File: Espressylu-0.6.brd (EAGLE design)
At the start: 101.6 x 76.2 mm, 135 parts, among them J1 4P-TERM-BLOCK284391-4, J10 MICROSD, J11 2x7, J2 M02POLAR, J3 M02POLAR, J4 USB-MICRO-PTH, J5 M02POLAR, J6 HOTEND-1, J7 HOTBED, J8 M02POLAR, J9 M02POLAR, P1 POLOLU-X, P2 POLOLU-Y, P3 POLOLU-Z, P4 POLOLU-E1, Q1 PMV45EN, Q2 PSMN1R8-40YLC, Q3 MMUN2211LT3G, Q4 PSMN1R8-40YLC, U1 DRTR5V0U2SR, U2 MCP1402T, U3 LMR16006X, U4 L78L15ABUTR, U5 MCP1402T, X1 12MHZ

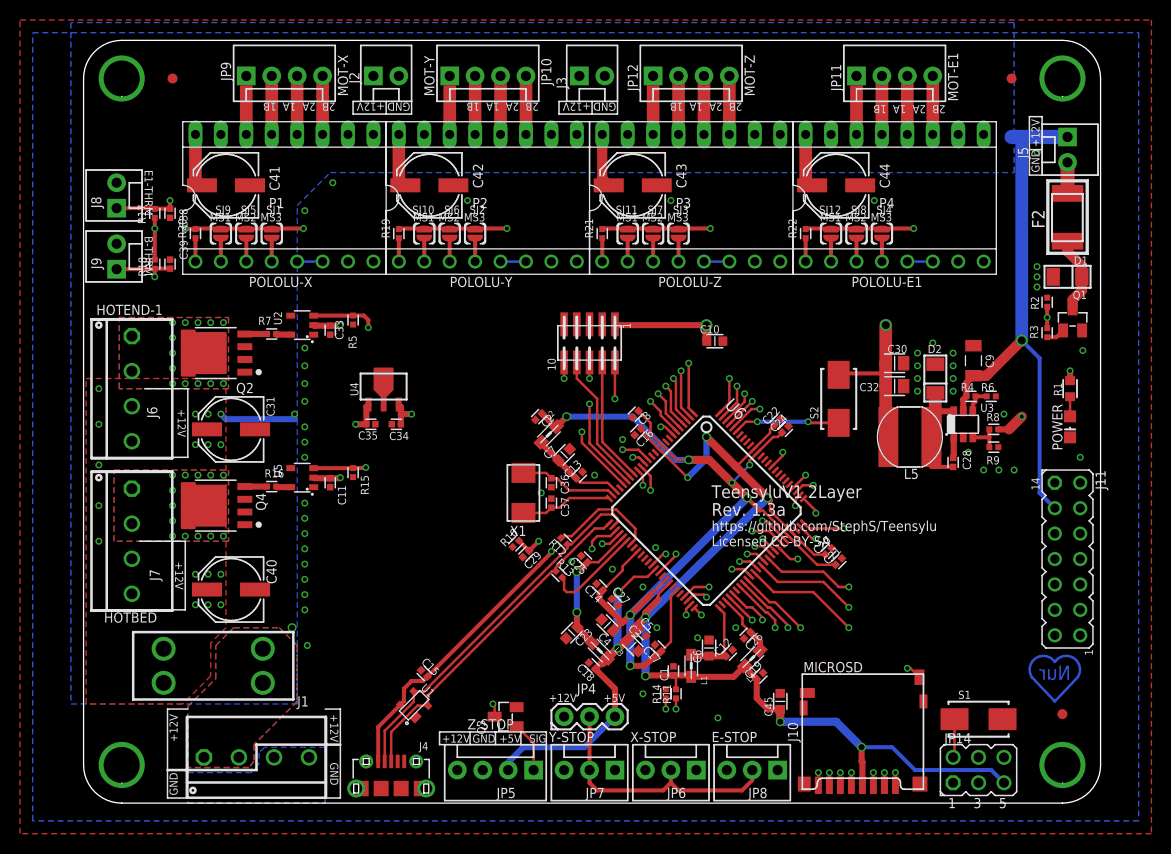
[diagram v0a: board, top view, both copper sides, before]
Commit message: Layout cleanup
Moved the stepper motor headers closer to the connectors. Cleaned up the
schematic and labels.
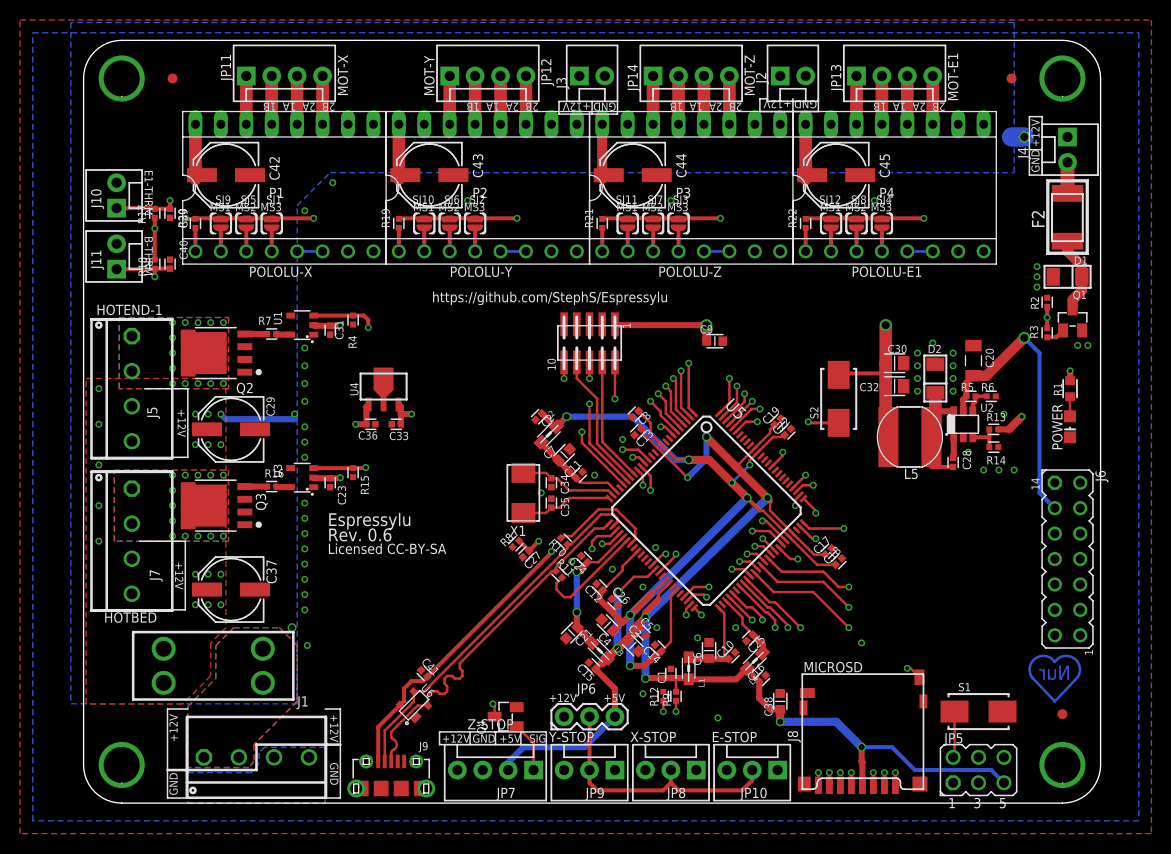
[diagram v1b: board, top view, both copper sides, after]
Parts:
- C10, C23: value 4.7uF -> 0.1uF; device teensylu:CAPC1608X92N -> teensylu:CAPC1005X60N
- C20: value 0.1uF -> 4.7uF; device teensylu:CAPC1005X60N -> teensylu:CAPC3215X168N
- C21: value 0.1uF -> 4.7uF; device teensylu:CAPC1005X60N -> teensylu:CAPC1608X92N
- C27: value 0.1uF -> 10pF
- C29: value 10pF -> 100uF; device teensylu:CAPC1005X60N -> teensylu:PANASONIC_D
- C31, C41: value 100uF -> 0.1uF; device teensylu:PANASONIC_D -> teensylu:CAPC1005X60N
- C33: value 0.1uF -> 1uF
- C34: value 1uF -> 15pF
- C35: value 0.1uF -> 15pF
- C36: value 15pF -> 0.1uF
- C37: value 15pF -> 100uF; device teensylu:CAPC1005X60N -> teensylu:PANASONIC_D
- C38: value 10uF -> 4.7uF; device teensylu:CAPC1005X60N -> teensylu:CAPC1608X92N
- C40: value 100uF -> 10uF; device teensylu:PANASONIC_D -> teensylu:CAPC1005X60N
- C45: value 4.7uF -> 100uF; device teensylu:CAPC1608X92N -> teensylu:PANASONIC_D
- C9: device teensylu:CAPC3215X168N -> teensylu:CAPC1608X92N
- J10: value MICROSD -> M02POLAR; device teensylu:AMPHENOL-MICROSD -> teensylu:MOLEX-1X2
- J11: value 2x7 -> M02POLAR; device teensylu:JP7Q -> teensylu:MOLEX-1X2
- J4: value USB-MICRO-PTH -> M02POLAR; device teensylu:USB-MICROB-PTH -> teensylu:MOLEX-1X2
- J5: value M02POLAR -> HOTEND-1; device teensylu:MOLEX-1X2 -> teensylu:284391-4
- J6: value HOTEND-1 -> 2x7; device teensylu:284391-4 -> teensylu:JP7Q
- J8: value M02POLAR -> MICROSD; device teensylu:MOLEX-1X2 -> teensylu:AMPHENOL-MICROSD
- J9: value M02POLAR -> USB-MICRO-PTH; device teensylu:MOLEX-1X2 -> teensylu:USB-MICROB-PTH
- JP10: value MOT-Y -> M03POLAR; device teensylu:MOLEX-1X4 -> teensylu:MOLEX-1X3
- JP11: value MOT-E1 -> MOT-X
- JP12: value MOT-Z -> MOT-Y
- JP13: value JTAG-HEADER -> MOT-E1; device teensylu:2X05-0.5-SMD -> teensylu:MOLEX-1X4
- JP14: value ISP -> MOT-Z; device teensylu:ISP -> teensylu:MOLEX-1X4
- JP4: value JUMPER-3PTH -> JTAG-HEADER; device teensylu:1X03 -> teensylu:2X05-0.5-SMD
- JP5: value Z-STOP -> ISP; device teensylu:MOLEX-1X4 -> teensylu:ISP
- JP6: value M03POLAR -> JUMPER-3PTH; device teensylu:MOLEX-1X3 -> teensylu:1X03
- JP7: value M03POLAR -> Z-STOP; device teensylu:MOLEX-1X3 -> teensylu:MOLEX-1X4
- JP9: value MOT-X -> M03POLAR; device teensylu:MOLEX-1X4 -> teensylu:MOLEX-1X3
- Q3: value MMUN2211LT3G -> PSMN1R8-40YLC; device teensylu:SOT23C -> teensylu:LFPACK-POWERPAK-SO8
- Q4: value PSMN1R8-40YLC -> MMUN2211LT3G; device teensylu:LFPACK-POWERPAK-SO8 -> teensylu:SOT23C
- R10: value 6.8k -> 39
- R11: value 100k -> 39
- R12: value 39 -> 0
- R13: value 39 -> 28k
- R14: value 0 -> 8.45k
- R4: value 15k -> 10k
- R5: value 10k -> 15k
- R8: value 28k -> 6.8k
- R9: value 8.45k -> 100k
- U1: value DRTR5V0U2SR -> MCP1402T; device teensylu:SOT143-R -> teensylu:SOT23-5
- U2: value MCP1402T -> LMR16006X; device teensylu:SOT23-5 -> teensylu:TSOT6
- U3: value LMR16006X -> MCP1402T; device teensylu:TSOT6 -> teensylu:SOT23-5
- U5: value MCP1402T -> (none); device teensylu:SOT23-5 -> teensylu:LQFP100
- U6: value (none) -> DRTR5V0U2SR; device teensylu:LQFP100 -> teensylu:SOT143-R
- moved J11 99.3 mm to (3.30, 53.3), turned to 90 degrees
- moved J5 96.8 mm to (4.83, 41.4)
- moved J6 95.0 mm to (98.3, 24.4)
- moved J4 93.8 mm to (98.3, 66.5), turned to 270 degrees
- moved J10 90.5 mm to (3.30, 59.4), turned to 90 degrees
- moved J8 90.5 mm to (77.5, 7.62), turned to 0 degrees
- moved JP9 78.5 mm to (53.1, 3.30), turned to 180 degrees
- moved C38 78.1 mm to (69.6, 10.2)
- moved JP10 76.7 mm to (69.3, 3.30), turned to 180 degrees
- moved JP14 76.6 mm to (56.9, 72.6)
- moved U2 66.8 mm to (87.9, 37.8), turned to 0 degrees
- moved U3 66.3 mm to (21.8, 32.5), turned to 90 degrees
- moved R4 62.2 mm to (26.9, 48.3), turned to 270 degrees
- moved R5 62.2 mm to (88.6, 40.6), turned to 0 degrees
- moved JP11 61.0 mm to (16.3, 72.6)
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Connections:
- net !E1-ENABLE: now also U5.98; no longer U6.98
- net !HOTBED: now also U3.3, U5.15; no longer U5.3, U6.15
- net !HOTEND-1: now also R4.1, U1.3, U5.14; no longer R5.1, U2.3, U6.14
- net !PWM-FAN: now also U5.85; no longer U6.85
- net !RESET: now also JP4.10, JP5.2, U5.47; no longer JP13.10, JP14.2, U6.47
- net !X-ENABLE: now also U5.7; no longer U6.7
- net !Y-ENABLE: now also U5.4; no longer U6.4
- net !Z-ENABLE: now also U5.1; no longer U6.1
- net +15V: now also C23.1, C31.1, C36.1, U1.2, U3.2; no longer C11.1, C33.1, C35.1, U2.2, U5.2
- net +3V3: now also C13.1, C15.1, C17.1, C26.1, C38.1, C9.1, J6.2, J8.4, JP4.1, JP5.5, JP6.3, JP7.2, R13.1, R9.2, U5.11, U5.39, U5.43, U5.72, U5.90; no longer C10.1, C18.1, C20.1, C22.1, C27.1, C45.1, J10.4, J11.2, JP13.1, JP14.5, JP4.3, JP5.2, R11.2, R8.1, U6.11, U6.39, U6.43, U6.72, U6.90
- net 24V: now also C20.1, C29.+, C33.1, C37.+, C45.+, J4.1, J5.3, J5.4, JP6.1, JP7.4, R5.1, U2.5; no longer C31.+, C34.1, C40.+, C41.+, C9.1, J11.3, J5.1, J6.4, JP4.1, JP5.4, R4.1, U3.5
- net 5VREG_CB: now also U2.1; no longer U3.1
- net 5VREG_FB: now also R13.2, R14.1, U2.3; no longer R8.2, R9.1, U3.3
- net 5VREG_SW: now also U2.6; no longer U3.6
- net AD3: now also J6.13, U5.60; no longer J11.13, U6.60
- net ADVREF: now also C25.1, U5.53; no longer C26.1, U6.53
- net B-THERM: now also C40.2, J11.1, U5.69; no longer C39.2, J9.1, U6.69
- net E-MOT-1A: now also JP13.3; no longer JP11.3
- net E-MOT-1B: now also JP13.4; no longer JP11.4
- net E-MOT-2A: now also JP13.2; no longer JP11.2
- net E-MOT-2B: now also JP13.1; no longer JP11.1
- net E-STOP: now also JP10.1, U5.55; no longer JP8.1, U6.55
- net E1-DIR: now also U5.96; no longer U6.96
- net E1-STEP: now also U5.97; no longer U6.97
- net E1-THERM: now also C39.2, J10.1, U5.70; no longer C38.2, J8.1, U6.70
- net ENDSTOP+V: now also JP10.2, JP9.2; no longer JP4.2, JP7.2
- net ERASE: now also U5.95; no longer U6.95
- net GND: now also C15.2, C29.-, C31.2, C34.1, C35.1, C36.2, C37.-, C38.2, C40.1, C41.1, C45.-, J10.2, J11.2, J6.1, J8.6, J8.C1, J8.C2, J8.C3, J8.C4, J8.CD1, J9.GND, J9.GND1, J9.GND2, J9.GND3, J9.GND4, J9.GND5, J9.GND6, J9.GND7, J9.GND8, JP10.3, JP4.3, JP4.5, JP4.9, JP5.1, JP9.3, Q3.1, Q3.3, R12.2, R4.2, R8.1, U1.4, U2.2, U3.1, U3.4, U5.12, U5.22, U5.33, U5.35, U5.41, U5.44, U5.52, U5.73, U5.91, U6.1; no longer C15.1, C29.2, C31.-, C34.2, C35.2, C36.1, C37.1, C38.1, C40.-, C41.-, C45.2, J10.6, J10.C1, J10.C2, J10.C3, J10.C4, J10.CD1, J11.1, J4.GND, J4.GND1, J4.GND2, J4.GND3, J4.GND4, J4.GND5, J4.GND6, J4.GND7, J4.GND8, J8.2, J9.2, JP13.3, JP13.5, JP13.9, JP14.1, JP5.3, JP6.3, Q4.1, Q4.3, R10.1, R5.2, R9.2, U2.1, U2.4, U3.2, U5.1, U5.4, U6.12, U6.22, U6.33, U6.35, U6.41, U6.44, U6.52, U6.73, U6.91
- net HOTBED-GND: now also Q3.5-8; no longer Q4.5-8
- net HOTEND-GND: now also J5.1, J5.2; no longer J6.1, J6.2
- net JTAG_TCK: now also JP4.4, U5.18; no longer JP13.4, U6.18
- net JTAG_TDI: now also JP4.8, U5.19; no longer JP13.8, U6.19
- net JTAG_TDO: now also JP4.6, U5.20; no longer JP13.6, U6.20
- net JTAG_TMS: now also JP4.2, U5.21; no longer JP13.2, U6.21
- net MCCDA: now also J8.3, U5.50; no longer J10.3, U6.50
- net MCCK: now also J8.5, U5.49; no longer J10.5, U6.49
- net MCDA0: now also J8.7, U5.74; no longer J10.7, U6.74
- net MCDA1: now also J8.8, U5.59; no longer J10.8, U6.59
- net MCDA2: now also J8.1, U5.58; no longer J10.1, U6.58
- net MCDA3: now also J8.2, U5.57; no longer J10.2, U6.57
- net MISO: now also JP5.6, U5.75; no longer JP14.6, U6.75
- net MOSI: now also JP5.3, U5.76; no longer JP14.3, U6.76
- net N$12: now also R11.2, U5.31; no longer R13.2, U6.31
- net N$14: now also U3.5; no longer U5.5
- net N$15: now also U1.5; no longer U2.5
- net N$2: now also Q3.4; no longer Q4.4
- net N$3: now also R5.2, U2.4; no longer R4.2, U3.4
- net N$4: now also R9.1, U5.40; no longer R11.1, U6.40
- net N$5: now also J4.2; no longer J5.2
- net N$7: now also R12.1, U5.38; no longer R14.1, U6.38
- net N$9: now also R10.2, U5.32; no longer R12.2, U6.32
- net PA15: now also U5.8; no longer U6.8
- net PA17: now also U5.9; no longer U6.9
- net PA2: now also J6.12, U5.63; no longer J11.12, U6.63
- net PA28: now also J6.5, U5.78; no longer J11.5, U6.78
- net PA29: now also J6.4, U5.79; no longer J11.4, U6.79
- net PA3: now also J6.11, U5.62; no longer J11.11, U6.62
- net PA4: now also J6.14, U5.61; no longer J11.14, U6.61
- net PB12: now also J6.9, U5.64; no longer J11.9, U6.64
- net PB13: now also J6.10, U5.65; no longer J11.10, U6.65
- net PB17: now also J6.8, U5.66; no longer J11.8, U6.66
- net PB18: now also J6.6, U5.67; no longer J11.6, U6.67
- net PB19: now also J6.7, U5.68; no longer J11.7, U6.68
- net SCLK: now also JP5.4, U5.77; no longer JP14.4, U6.77
- net SDCD: now also J8.CD2, U5.48; no longer J10.CD2, U6.48
- net USB_DN: now also J9.D-, R10.1, U5.27, U6.3; no longer J4.D-, R12.1, U1.3, U6.27
- net USB_DP: now also J9.D+, R11.1, U5.26, U6.2; no longer J4.D+, R13.1, U1.2, U6.26
- net VBG: now also C27.1, R8.2, U5.29; no longer C29.1, R10.2, U6.29
- net VBUS: now also C41.2, J9.VBUS, U5.28, U6.4; no longer C15.2, J4.VBUS, U1.4, U6.28
- net VDD: now also C12.1, C18.1, C22.1, U5.10, U5.34, U5.42, U5.45, U5.71, U5.89; no longer C17.1, C21.1, C24.1, U6.10, U6.34, U6.42, U6.45, U6.71, U6.89
- net VDDANA: now also C10.1, U5.51; no longer C12.1, U6.51
- net VDDPLL: now also C11.1, U5.23; no longer C13.1, U6.23
- net VDDUTMI: now also C21.1, C24.1, U5.30; no longer C23.1, C25.1, U6.30
- net X-DIR: now also U5.5; no longer U6.5
- net X-MOT-1A: now also JP11.3; no longer JP9.3
- net X-MOT-1B: now also JP11.4; no longer JP9.4
- net X-MOT-2A: now also JP11.2; no longer JP9.2
- net X-MOT-2B: now also JP11.1; no longer JP9.1
- net X-STEP: now also U5.6; no longer U6.6
- net X-STOP: now also JP8.1, U5.54; no longer JP6.1, U6.54
- net XTAL1: now also C35.2, U5.25; no longer C37.2, U6.25
- net XTAL2: now also C34.2, U5.24; no longer C36.2, U6.24
- net Y-DIR: now also U5.2; no longer U6.2
- net Y-MOT-1A: now also JP12.3; no longer JP10.3
- net Y-MOT-1B: now also JP12.4; no longer JP10.4
- net Y-MOT-2A: now also JP12.2; no longer JP10.2
- net Y-MOT-2B: now also JP12.1; no longer JP10.1
- net Y-STEP: now also U5.3; no longer U6.3
- net Y-STOP: now also JP9.1, U5.16; no longer JP7.1, U6.16
- net Z-DIR: now also U5.99; no longer U6.99
- net Z-MOT-1A: now also JP14.3; no longer JP12.3
- net Z-MOT-1B: now also JP14.4; no longer JP12.4
- net Z-MOT-2A: now also JP14.2; no longer JP12.2
- net Z-MOT-2B: now also JP14.1; no longer JP12.1
- net Z-STEP: now also U5.100; no longer U6.100
- net Z-STOP: now also Q4.3, U5.17; no longer Q3.3, U6.17
- net Z-STOP-BIAS: now also JP7.1, Q4.1; no longer JP5.1, Q3.1
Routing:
- net 24V: track 134.8 -> 138.4 mm, vias 21 -> 22
- net +3V3: track 417.8 -> 421.0 mm
- net USB_DP: track 34.2 -> 37.1 mm
- net E1-THERM: track 86.5 -> 84.9 mm
- net N$12: track 9.81 -> 11.2 mm
- net Z-STEP: track 16.7 -> 17.7 mm
- net Z-DIR: track 17.9 -> 19.0 mm
- net Y-DIR: track 20.3 -> 21.3 mm
- net !Z-ENABLE: track 21.3 -> 22.4 mm
- net !E1-ENABLE: track 21.5 -> 22.6 mm
- net Z-MOT-2B: track 5.84 -> 4.83 mm
- net Z-MOT-2A: track 5.84 -> 4.83 mm
- net Z-MOT-1B: track 5.84 -> 4.83 mm
- net Z-MOT-1A: track 5.84 -> 4.83 mm
- net Y-MOT-2B: track 5.84 -> 4.83 mm
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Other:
- board text added: "Espressylu"
- board text added: "Rev. 0.6"
- board text added: "https://github.com/StephS/Espressylu"
- board text removed: "Rev. 1.3a"
- board text removed: "TeensyluV1 2Layer"
- board text removed: "https://github.com/StephS/Teensylu"
